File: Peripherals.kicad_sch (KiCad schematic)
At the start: 0 parts

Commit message: Worked on peripheral schem
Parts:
- added C1: 10uF, PCM_JLCPCB:C_0603, symbol PCM_JLCPCB-Capacitors:0603,10uF
- added C2, C4, C5, C6, C7, C8, C9: 100nF, PCM_JLCPCB:C_0603, symbol PCM_JLCPCB-Capacitors:0603,100nF
- added C3: 4.7uF, PCM_JLCPCB:C_0603, symbol PCM_JLCPCB-Capacitors:0603,4.7uF
- added R1, R2, R3, R4, R5: 4.7kΩ, PCM_JLCPCB:R_0603, symbol PCM_JLCPCB-Resistors:0603,4.7kΩ
- added R6, R7, R8: 10kΩ, PCM_JLCPCB:R_0603, symbol PCM_JLCPCB-Resistors:0603,10kΩ
- added U1: MAX30102, OptoDevice:Maxim_OLGA-14_3.3x5.6mm_P0.8mm, symbol Sensor:MAX30102
- added U2: BMI270, BMI270_BOS, symbol 2026-04-08_00-20-06:BMI270
- added U3: OPT3004DNPR, DNP0006A, symbol 2026-04-08_01-09-15:OPT3004DNPR
- added U4: LPS22DF, Package_LGA:ST_HLGA-10_2x2mm_P0.5mm_LayoutBorder3x2y, symbol Sensor_Pressure:LPS22DF
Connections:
- new net 1V8: C1.1, C2.1, C3.1, C4.1, C5.1, C6.1, C7.1, C8.1, C9.1, R3.2, R4.2, R5.2, R6.1, R7.1, R8.1, U1.10 (VLED+), U1.11 (VDD), U1.9 (VLED+), U2.12 (CSB), U2.5 (VDDIO), U2.8 (VDD), U3.1 (VDD), U4.1 (Vdd_IO), U4.10 (VDD)
- new net BMI_INT1: U2.9 (INT2)
- new net BMI_INT2: U2.4 (INT1)
- new net GND: C1.2, C2.2, C3.2, C4.2, C5.2, C6.2, C7.2, C8.2, C9.2, U1.12 (GND), U1.4 (PGND), U2.6 (GNDIO), U2.7 (GND), U3.2 (ADDR), U3.3 (GND), U3.7 (PAD), U4.3 (GND), U4.8 (GND_IO), U4.9 (GND)
- new net LPS_INT: U4.7 (INT_DRDY)
- new net MAX_INT: R3.1, U1.13 (~{INT})
- new net OPT_INT: R8.2, U3.5 (INT)
- new net SA0: U2.1 (SDO), U4.5 (SA0)
- new net SCL: R1.2, R4.1, R6.2, U1.2 (SCL), U2.13 (SCX), U3.4 (SCL), U4.2 (SCL)
- new net SDA: R2.2, R5.1, R7.2, U1.3 (SDA), U2.14 (SDX), U3.6 (SDA), U4.4 (SDA)
- new net VDD: R1.1, R2.1
- no-connect marks 0 -> 5
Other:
- note added: "AMB_LIGHT"
- note added: "BAROMETER"
- note added: "HEART RATE"
- note added: "IMU"

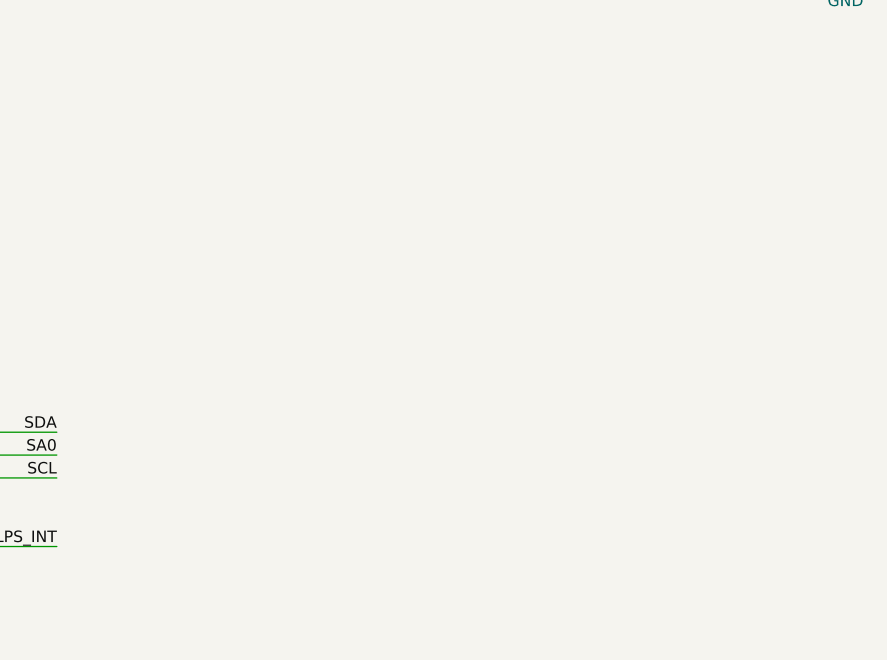
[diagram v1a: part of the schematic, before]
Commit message: Added flash
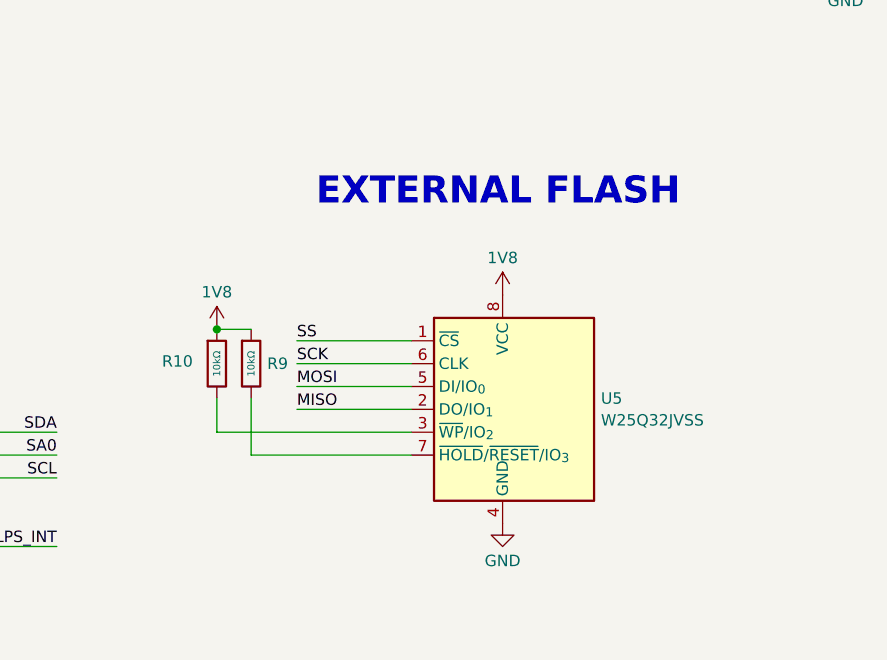
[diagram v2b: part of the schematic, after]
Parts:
- added R10, R9: 10kΩ, PCM_JLCPCB:R_0603, symbol PCM_JLCPCB-Resistors:0603,10kΩ
- added U5: W25Q32JVSS, Package_SO:SOIC-8_5.3x5.3mm_P1.27mm, symbol Memory_Flash:W25Q32JVSS
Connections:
- net 1V8: now also R10.1, R9.1, U5.8 (VCC)
- net GND: now also U5.4 (GND)
- new net: R9.2, U5.7 (~{HOLD}/~{RESET}/IO_{3})
- new net: R10.2, U5.3 (~{WP}/IO_{2})
- new net MISO: U5.2 (DO/IO_{1})
- new net MOSI: U5.5 (DI/IO_{0})
- new net SCK: U5.6 (CLK)
- new net SS: U5.1 (~{CS})
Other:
- note added: "EXTERNAL FLASH"

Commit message: Updated MCU
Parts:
- removed R10, R9: 10kΩ, PCM_JLCPCB:R_0603, symbol PCM_JLCPCB-Resistors:0603,10kΩ
- added C21: 100nF, PCM_JLCPCB:C_0603, symbol PCM_JLCPCB-Capacitors:0603,100nF
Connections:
- net 1V8: now also C21.1
- net GND: now also U2.1 (SDO), C21.2
- net SA0: no longer U2.1 (SDO)
- net QSPI_IO3: now reaches U5.7 (~{HOLD}/~{RESET}/IO_{3})
- net QSPI_IO2: now reaches U5.3 (~{WP}/IO_{2})
- net BMI_INT1 renamed BMI_INT
- net BMI_INT2: no longer names the net of U2.4 (INT1)
- net MISO renamed QSPI_IO1
- net MOSI renamed QSPI_IO0
- net SCK renamed QSPI_CLK
- net SS renamed QSPI_CS
- no-connect marks 5 -> 6

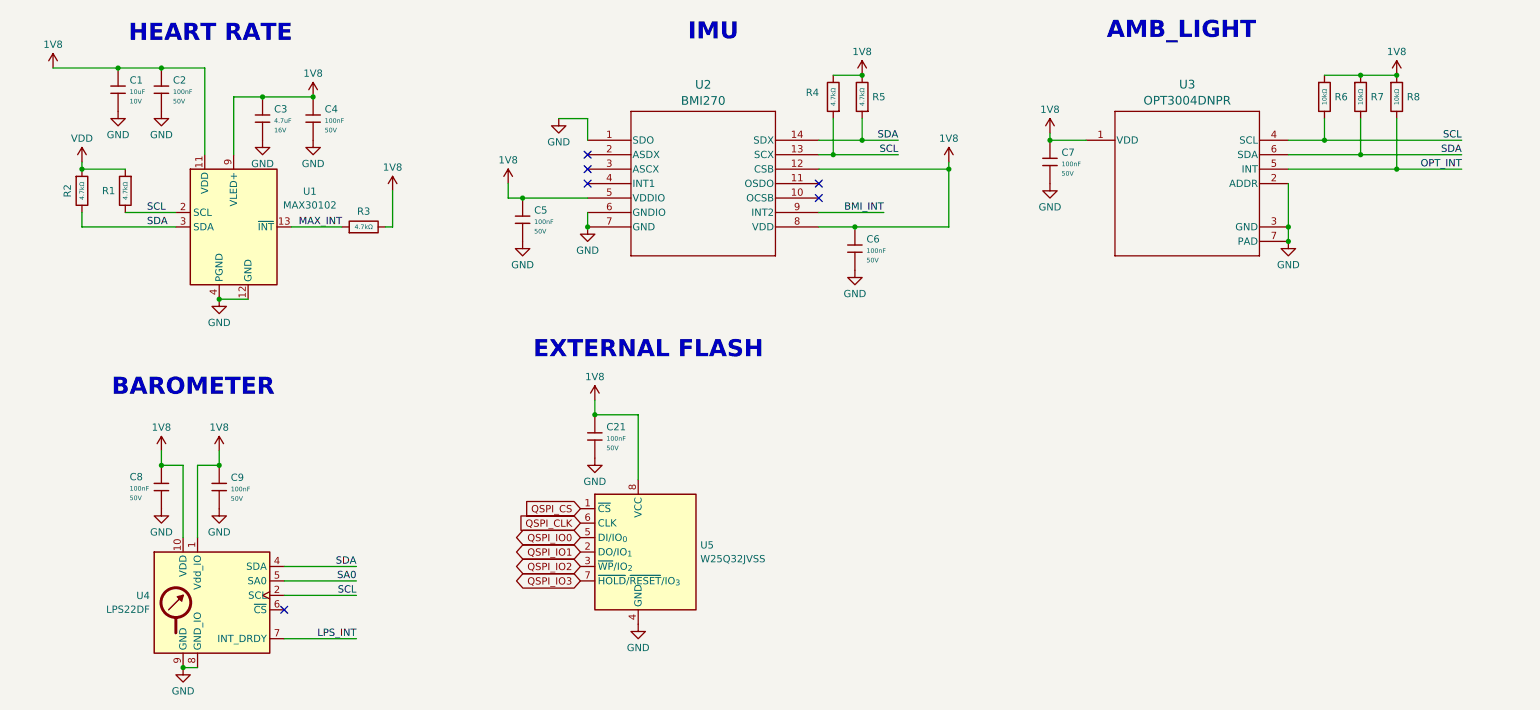
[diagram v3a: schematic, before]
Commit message: Fixed Hierarchical Labels
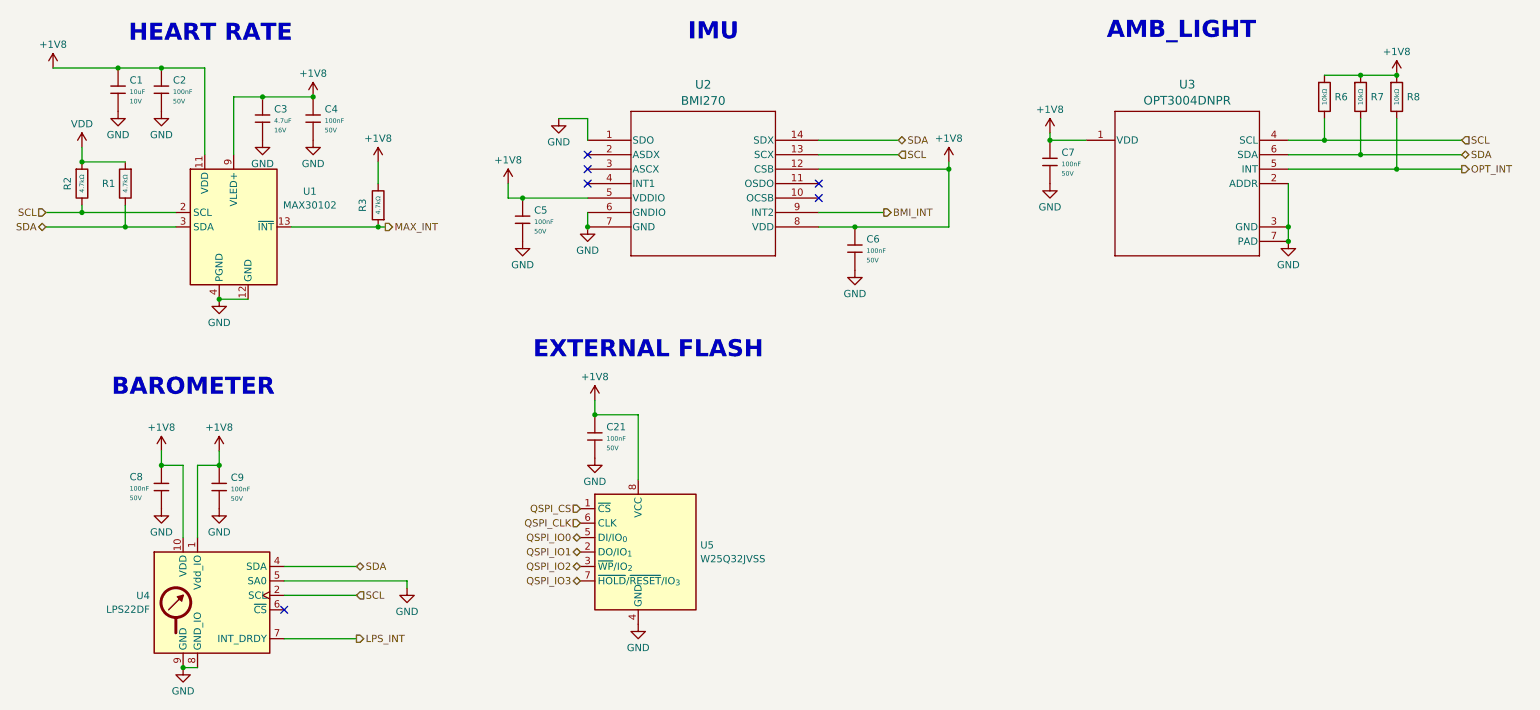
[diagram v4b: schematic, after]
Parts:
- removed R4, R5: 4.7kΩ, PCM_JLCPCB:R_0603, symbol PCM_JLCPCB-Resistors:0603,4.7kΩ
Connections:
- net SA0 is gone; now on net GND: U4.5 (SA0)
- net SCL: now also R2.2; no longer R1.2
- net SDA: now also R1.2; no longer R2.2
- net 1V8 renamed +1V8
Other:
- moved on the sheet: R1, R2, R3

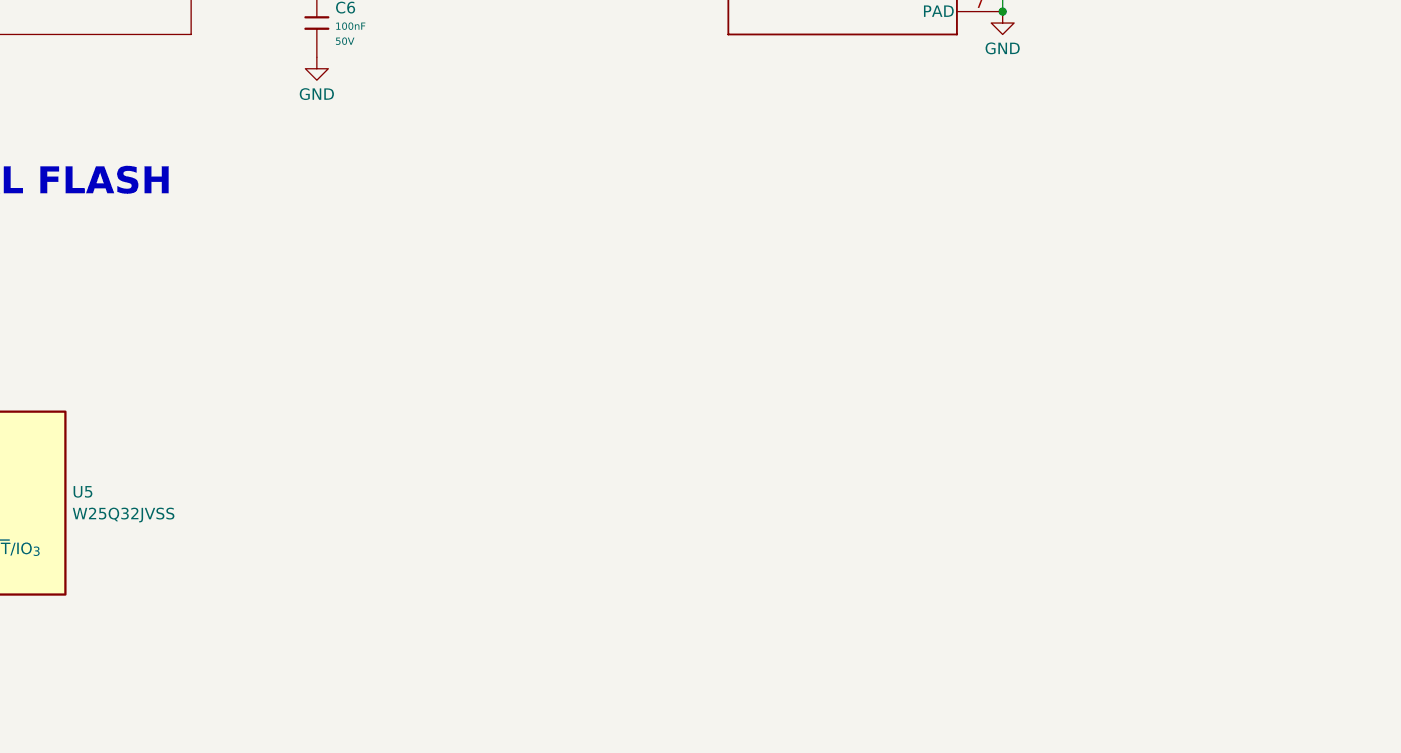
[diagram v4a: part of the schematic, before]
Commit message: Added Vibration Motor & Prog Pinout
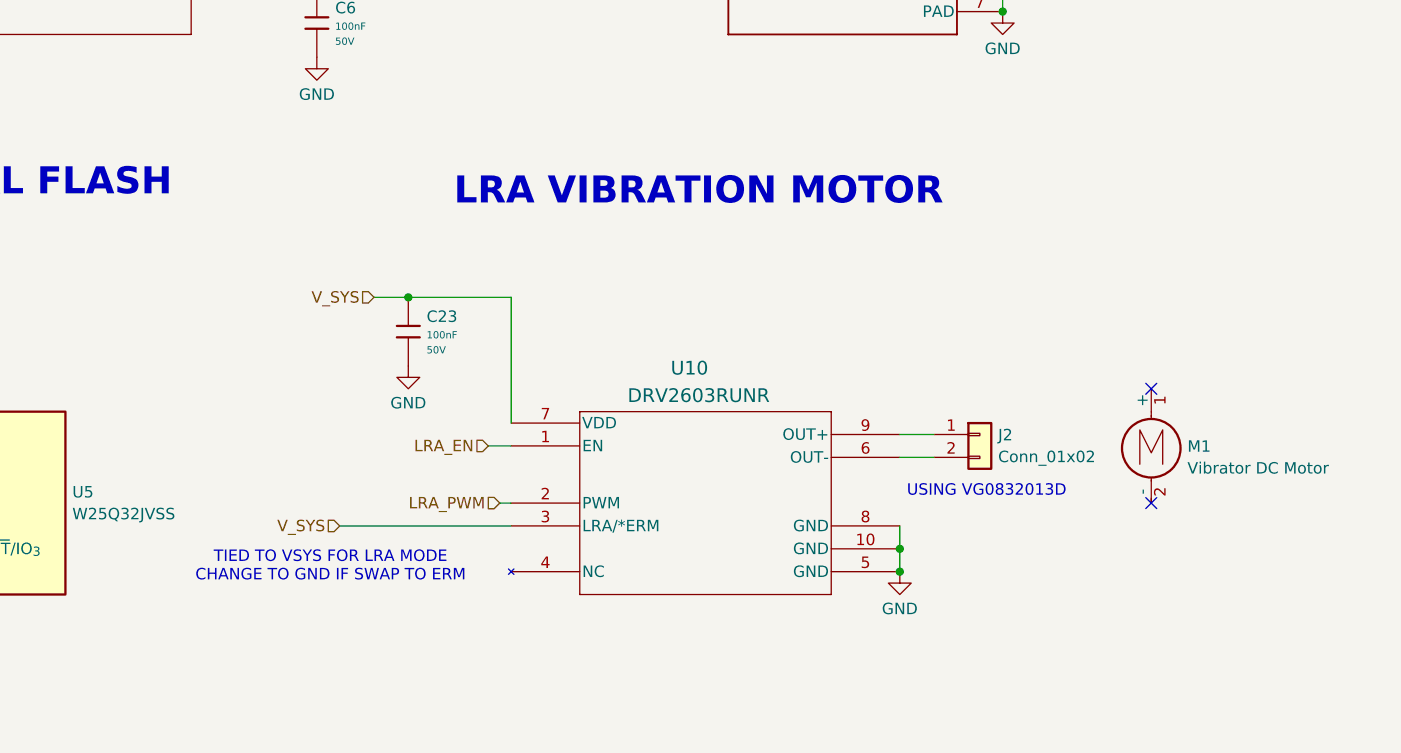
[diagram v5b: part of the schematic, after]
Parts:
- added C23: 100nF, PCM_JLCPCB:C_0603, symbol PCM_JLCPCB-Capacitors:0603,100nF
- added J2: Conn_01x02, symbol Connector_Generic:Conn_01x02
- added M1: Vibrator DC Motor, symbol Motor:Motor_DC
- added U10: DRV2603RUNR, RUN10_TEX, symbol 2026-04-14_20-16-38:DRV2603RUNR
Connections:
- net GND: now also C23.2, U10.10 (GND), U10.5 (GND), U10.8 (GND)
- new net: J2.1 (Pin_1), U10.9 (OUT+)
- new net: J2.2 (Pin_2), U10.6 (OUT-)
- new net LRA_EN: U10.1 (EN)
- new net LRA_PWM: U10.2 (PWM)
- new net V_SYS: C23.1, U10.3 (LRA/*ERM), U10.7 (VDD)
- no-connect marks 6 -> 8
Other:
- note added: "LRA VIBRATION MOTOR"
- note added: "TIED TO VSYS FOR LRA MODE CHANGE TO GND IF SWAP TO ERM"
- note added: "USING VG0832013D"

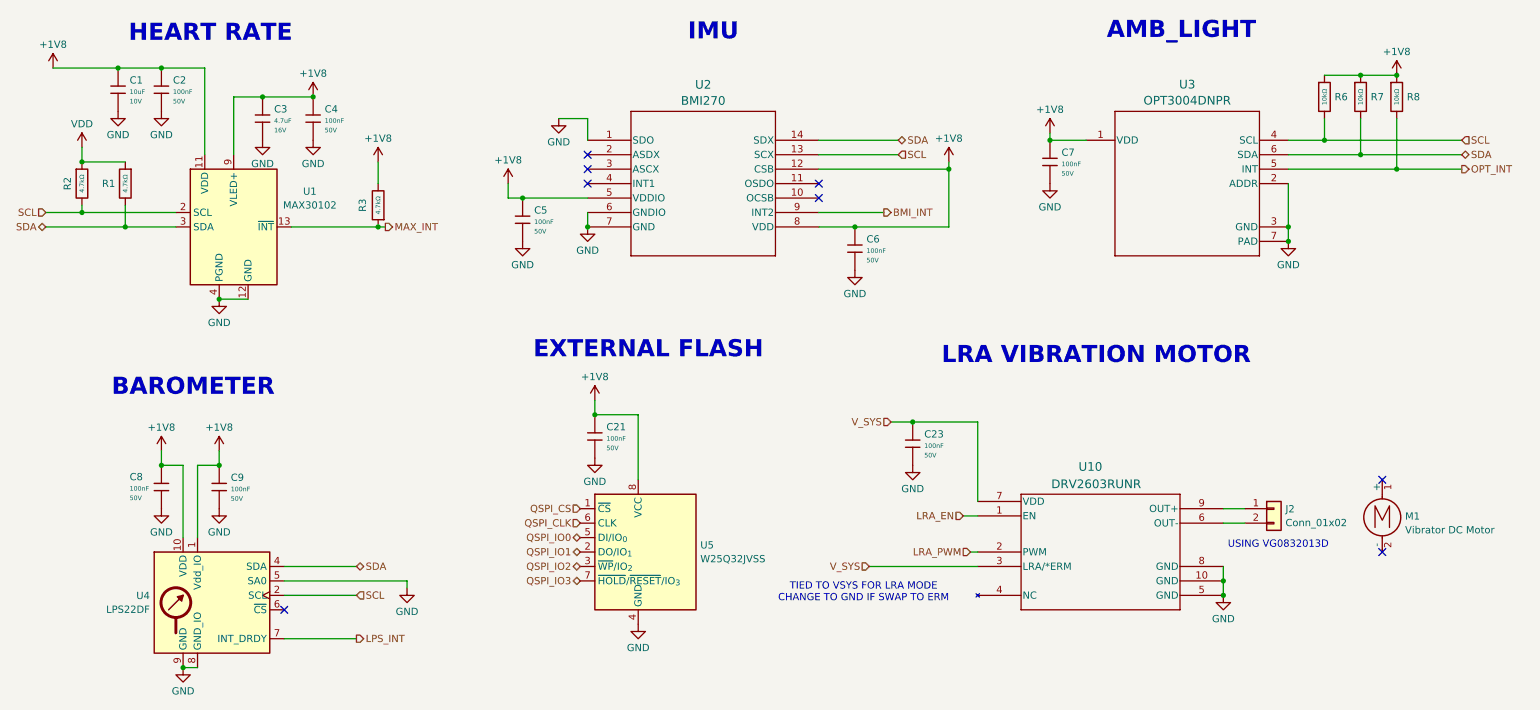
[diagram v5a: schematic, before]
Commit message: Added clock and updated schem
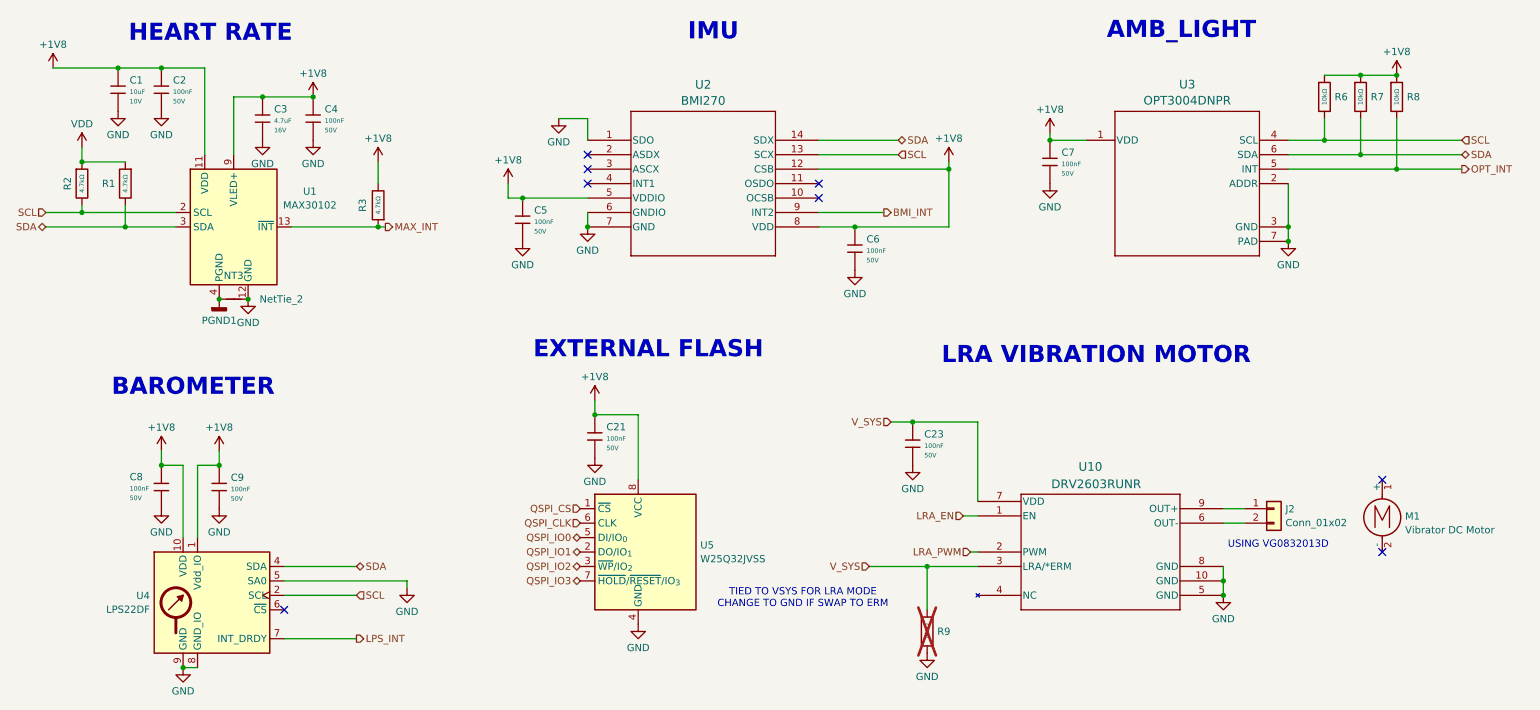
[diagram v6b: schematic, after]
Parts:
- added NT3: NetTie_2, symbol Device:NetTie_2
- added R9: 10kΩ, PCM_JLCPCB:R_0402, symbol PCM_JLCPCB-Resistors:0402,10kΩ
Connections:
- net GND: now also NT3.2, R9.2; no longer U1.4 (PGND)
- net V_SYS: now also R9.1
- new net PGND1: NT3.1, U1.4 (PGND)

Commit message: Updated Schem and Organized Layout
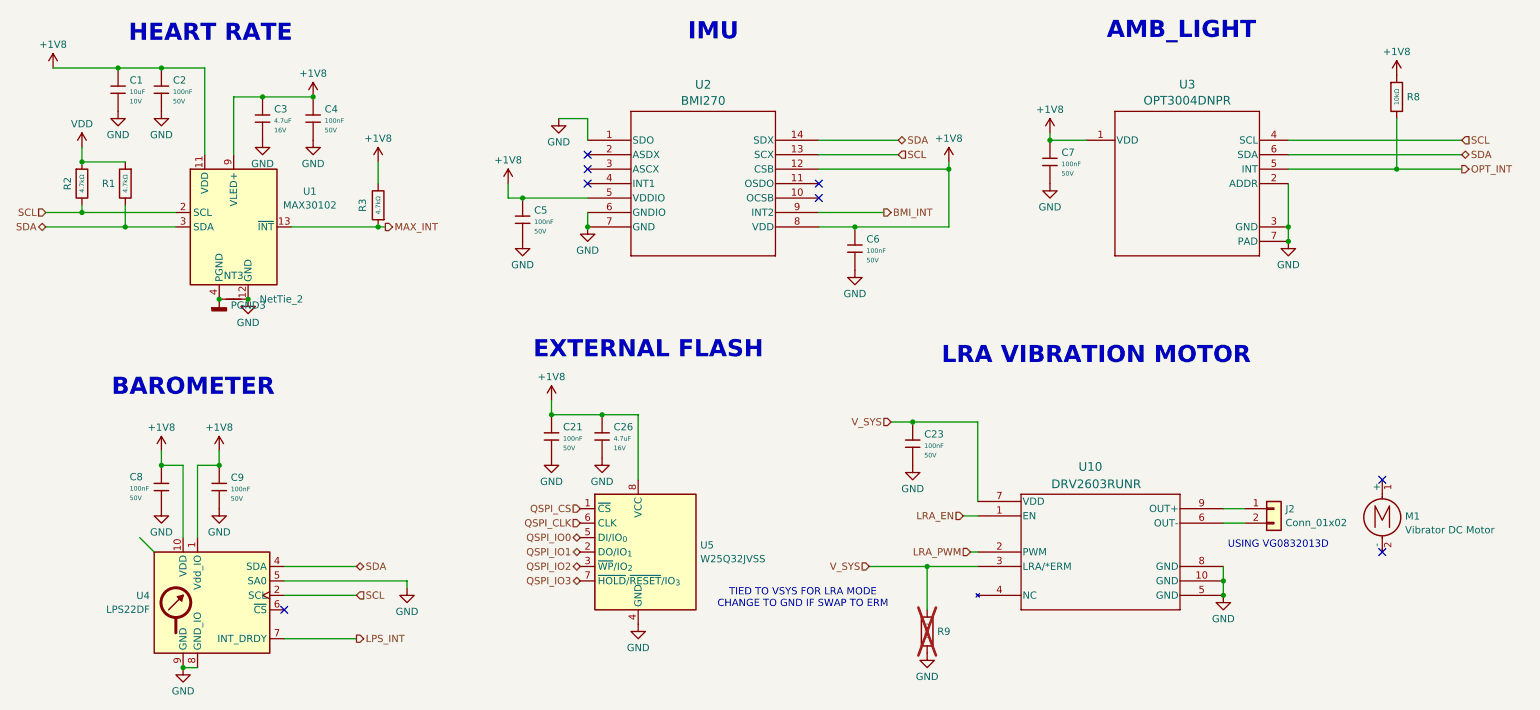
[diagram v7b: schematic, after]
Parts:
- removed R6, R7: 10kΩ, PCM_JLCPCB:R_0603, symbol PCM_JLCPCB-Resistors:0603,10kΩ
- added C26: 4.7uF, PCM_JLCPCB:C_0603, symbol PCM_JLCPCB-Capacitors:0603,4.7uF
- C1, C3: Manufacturer Samsung Electro-Mechanics -> (none)
- C2, C21, C23, C4, C5, C6, C7, C8, C9: Manufacturer YAGEO -> (none)
- J2: footprint (none) -> PAD_CONNECTOR:1x02_1x1mm
- NT3: footprint (none) -> NetTie:NetTie-2_SMD_Pad0.5mm
- R1, R2, R3, R8, R9: Manufacturer UNI-ROYAL(Uniroyal Elec) -> (none)
- U10: footprint RUN10_TEX -> DRV:RUN10_TEX
- U2: footprint BMI270_BOS -> BMI:BMI270_BOS
- U3: footprint DNP0006A -> OPT:DNP0006A
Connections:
- net +1V8: now also C26.1
- net GND: now also C26.2
- net PGND1 renamed PGND3
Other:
- moved on the sheet: C21
